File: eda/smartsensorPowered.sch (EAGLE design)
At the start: 36 parts, among them Q1 IRFML8244, Q2 IRFML8244, Q3 IRFML8244, Q4 IRFML8244, U1 ISL83491SOIC, U2 ATTINY1634

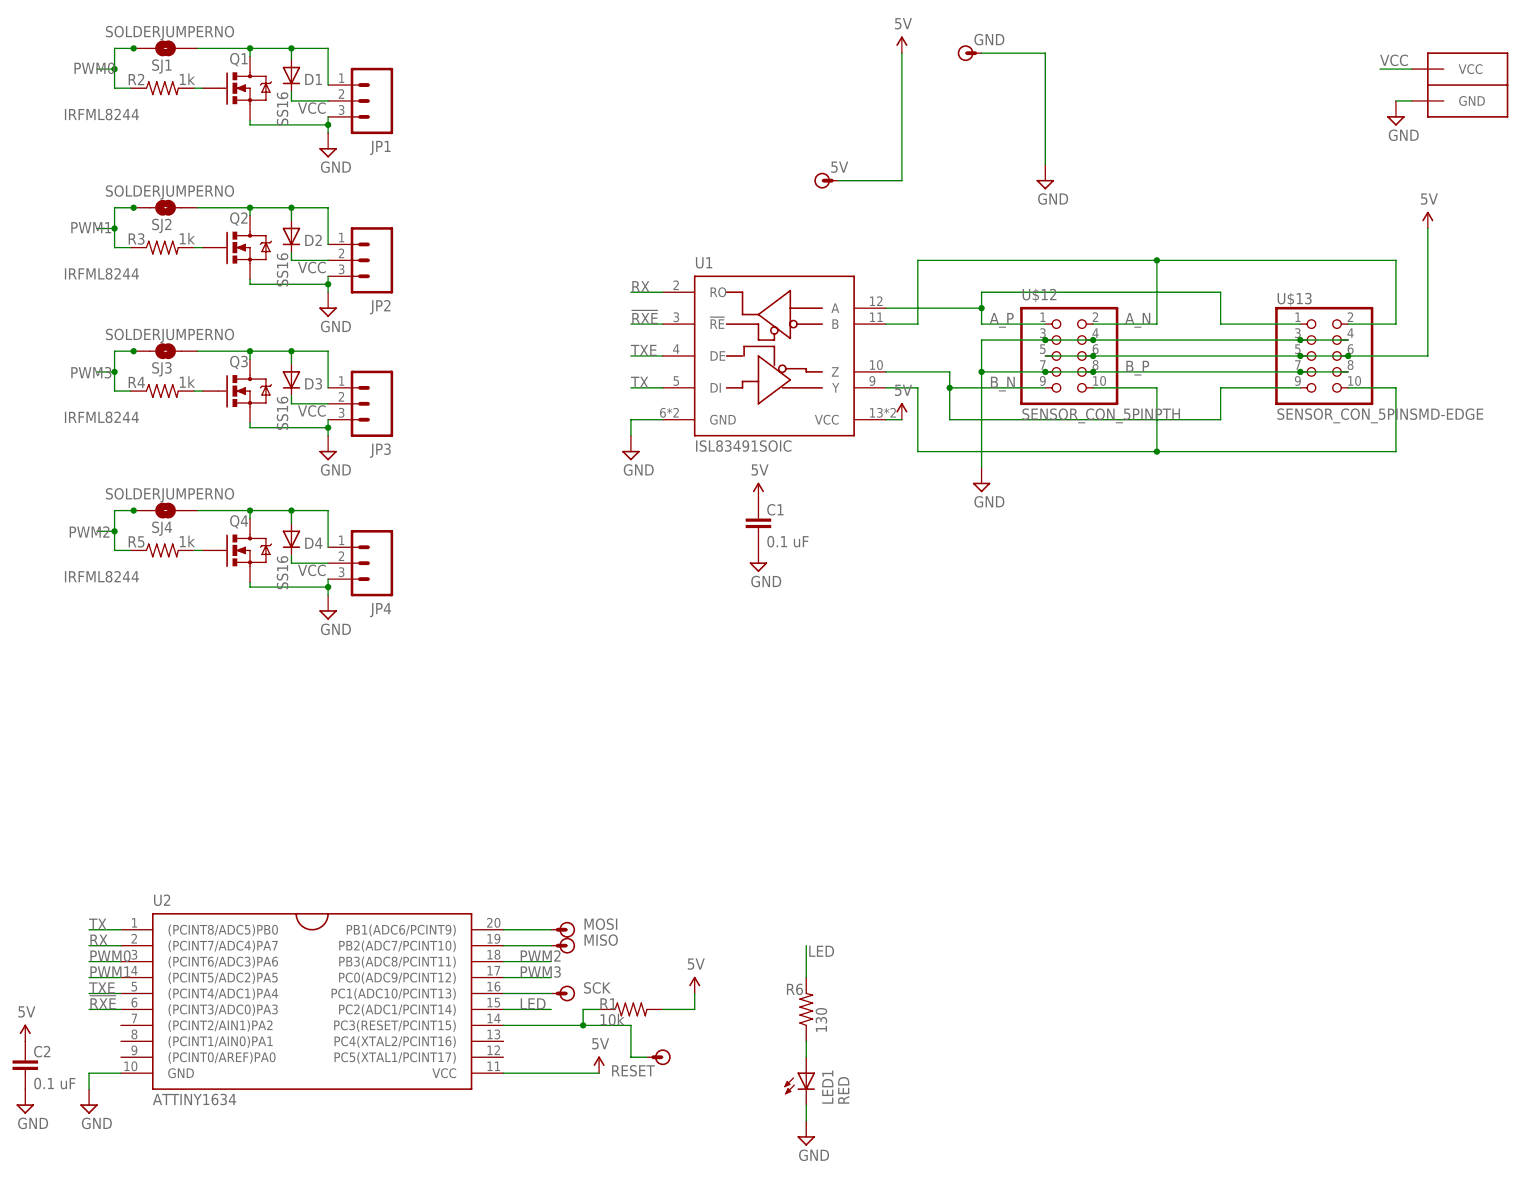
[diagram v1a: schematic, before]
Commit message: Add koala buck regulator to powered smart device and update everything for version 4
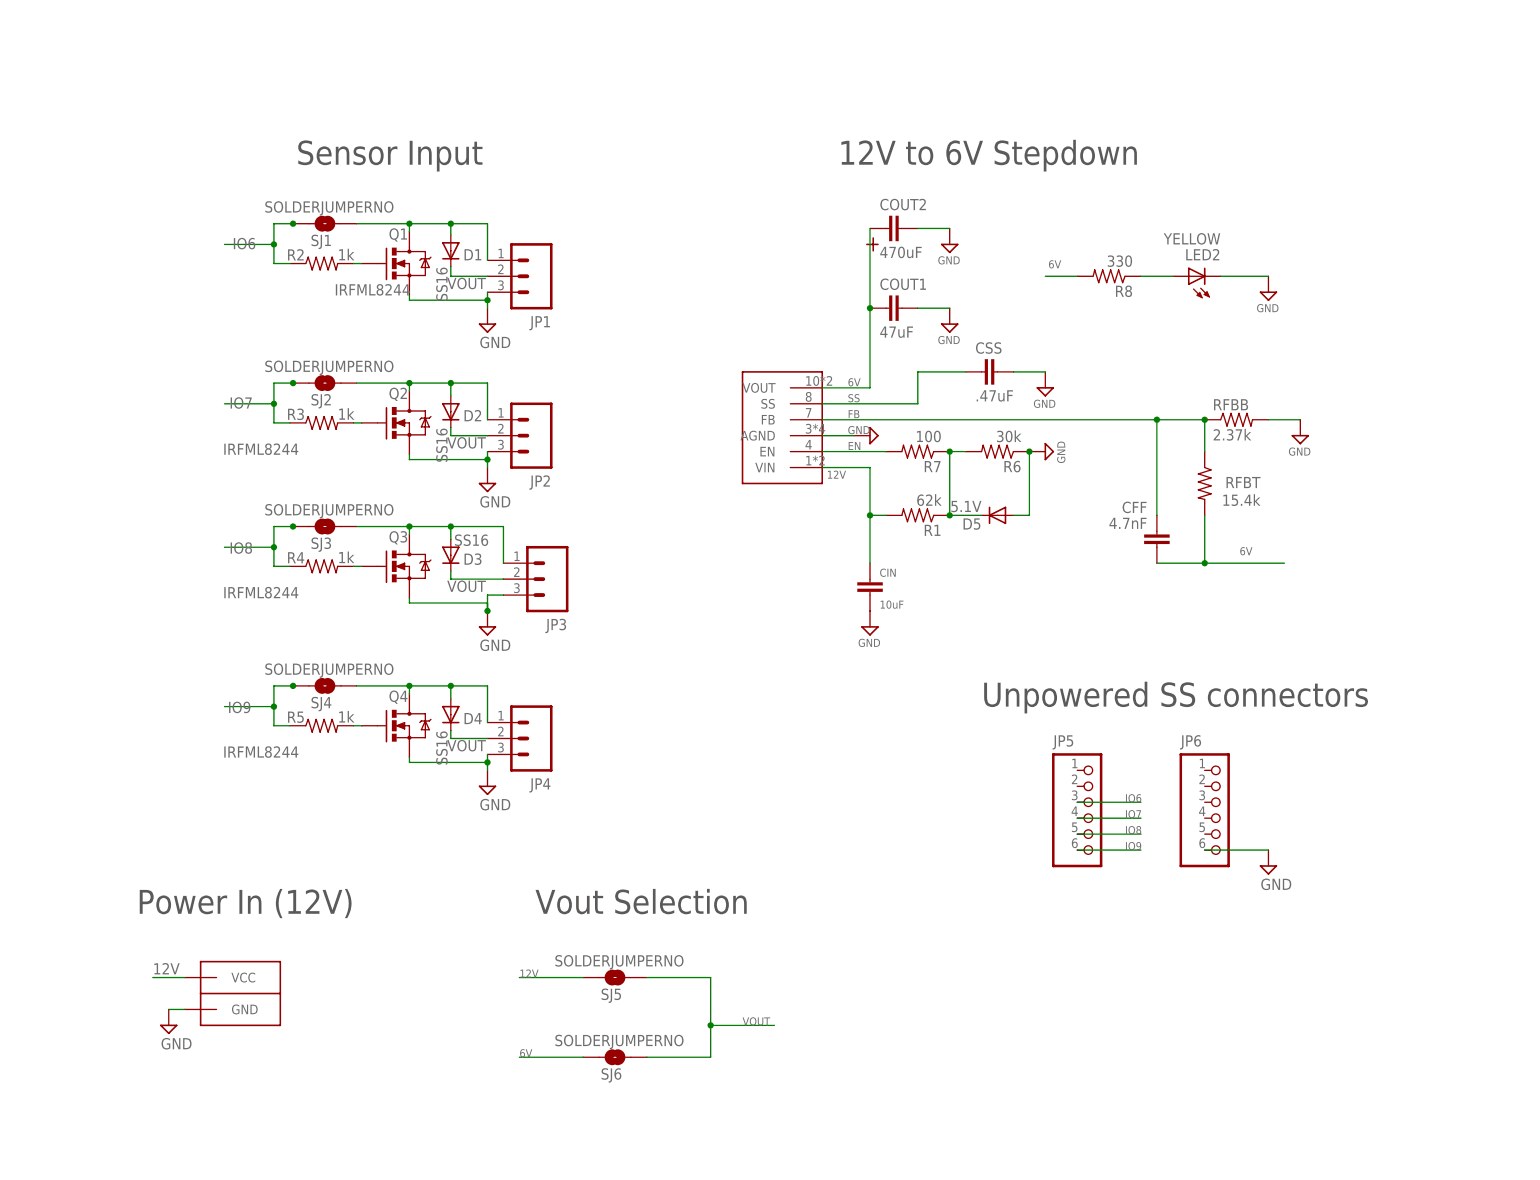
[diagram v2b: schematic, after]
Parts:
- removed 5V, GND, MISO, MOSI, RESET, SCK: (no value), pie:POGO_PIN
- removed C1, C2: 0.1 uF, pie:CAP0603-CAP
- removed LED1: RED, pie:LED0805
- removed U$12: SENSOR_CON_5PINPTH, pie:SENSOR_CON_5PINPTH-SHROUDED
- removed U$13: SENSOR_CON_5PINSMD-EDGE, pie:SENSOR_CON_5PINSMD-EDGE
- removed U1: ISL83491SOIC, pie:ISL83491SOIC
- removed U2: ATTINY1634, pie:ATTINY1634
- added CFF: 4.7nF, pie:CAP0603-CAP
- added CIN: 10uF, pie:CAP1206
- added COUT1: 47uF, pie:CAP1206
- added COUT2: 470uF, pie:TANT_CASE_E
- added CSS: .47uF, pie:CAP0603-CAP
- added D5: 5.1V, pie:DIODESOD-323
- added JP5, JP6: (no value), pie:PINHD-1X6
- added LED2: YELLOW, pie:LED0805
- added R7: 100, pie:R-US_R0603
- added R8: 330, pie:R-US_R0603
- added RFBB: 2.37k, pie:R-US_R0603
- added RFBT: 15.4k, pie:R-US_R0603
- added SJ5, SJ6: SOLDERJUMPERNO, pie:SOLDERJUMPERNO
- added U$3: LMZ12010, pie:LMZ12010
- R1: value 10k -> 62k
- R6: value 130 -> 30k
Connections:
- removed net !RXE: U1.!RE, U2.(PCINT3/ADC0)PA3
- removed net 5V: 5V.P$1, C1.1, C2.1, R1.2, U$12.5, U$12.6, U$13.5, U$13.6, U1.VCC, U2.VCC
- removed net A_N: U$12.2, U$13.2, U1.B
- removed net A_P: U$12.1, U$13.1, U1.A
- removed net B_N: U$12.9, U$13.9, U1.Z
- removed net B_P: U$12.10, U$13.10, U1.Y
- removed net LED: R6.2, U2.PC2(ADC1/PCINT14)
- removed net N$12: SCK.P$1, U2.PC1(ADC10/PCINT13)
- removed net N$6: MOSI.P$1, U2.PB1(ADC6/PCINT9)
- removed net N$9: MISO.P$1, U2.PB2(ADC7/PCINT10)
- removed net PWM0: R2.1, SJ1.1, U2.(PCINT6/ADC3)PA6
- removed net PWM1: R3.1, SJ2.1, U2.(PCINT5/ADC2)PA5
- removed net PWM2: R5.1, SJ4.1, U2.PB3(ADC8/PCINT11)
- removed net PWM3: R4.1, SJ3.1, U2.PC0(ADC9/PCINT12)
- removed net RESET: R1.1, RESET.P$1, U2.PC3(RESET/PCINT15)
- removed net RX: U1.RO, U2.(PCINT7/ADC4)PA7
- removed net TX: U1.DI, U2.(PCINT8/ADC5)PB0
- removed net TXE: U1.DE, U2.(PCINT4/ADC1)PA4
- removed net VCC: CONN1.VCC, D1.C, D2.C, D3.C, D4.C, JP1.2, JP2.2, JP3.2, JP4.2
- new net 12V: CIN.1, CONN1.VCC, R1.2, SJ5.1, U$3.VIN
- new net 6V: CFF.1, COUT1.1, COUT2.POS, R8.2, RFBT.2, SJ6.1, U$3.VOUT
- new net DIODE: D5.C, R1.1, R6.2, R7.1
- new net EN: R7.2, U$3.EN
- new net FB: CFF.2, RFBB.1, RFBT.1, U$3.FB
- new net IO6: JP5.3, R2.1, SJ1.1
- new net IO7: JP5.4, R3.1, SJ2.1
- new net IO8: JP5.5, R4.1, SJ3.1
- new net IO9: JP5.6, R5.1, SJ4.1
- new net SS: CSS.1, U$3.SS
- new net VOUT: D1.C, D2.C, D3.C, D4.C, JP1.2, JP2.2, JP3.2, JP4.2, SJ5.2, SJ6.2
- net GND: now also CIN.2, COUT1.2, COUT2.NEG, CSS.2, D5.A, JP6.6, LED2.C, R6.1, RFBB.2, U$3.AGND; no longer C1.2, C2.2, GND.P$1, LED1.C, U$12.3, U$12.4, U$12.7, U$12.8, U$13.3, U$13.4, U$13.7, U$13.8, U1.GND, U2.GND
- net N$3: now also LED2.A, R8.1; no longer LED1.A, R6.1
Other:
- note added: "12V to 6V Stepdown"
- note added: "Power In (12V)"
- note added: "Sensor Input"
- note added: "Unpowered SS connectors"
- note added: "Vout Selection"
- moved on the sheet: D1, D2, D3, D4, JP1, JP2, JP3, JP4, Q1, Q2, Q3, Q4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

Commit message: Fix smartsensorPowered brd and sch #2 - renamed N$1 N$2 N$3 N$4 wires with 6V_IF_SERVO1 6V_If_SERVO2 and so on - ripped up the trace from cout1 to GND -
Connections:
- net N$1 renamed 6V_IF_SERVO1
- net N$10 renamed 6V_IF_SERVO4
- net N$4 renamed 6V_IF_SERVO2
- net N$7 renamed 6V_IF_SERVO3
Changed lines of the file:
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@@
 </segment>
 </net>
-<net name="N$1" class="0">
+<net name="6V_IF_SERVO1" class="0">
 <segment>
 <pinref part="JP1" gate="G$1" pin="1"/>
@@
 </segment>
 </net>
-<net name="N$4" class="0">
+<net name="6V_IF_SERVO2" class="0">
 <segment>
 <pinref part="JP2" gate="G$1" pin="1"/>
@@
 </segment>
 </net>
-<net name="N$7" class="0">
+<net name="6V_IF_SERVO3" class="0">
 <segment>
 <pinref part="JP3" gate="G$1" pin="1"/>
@@
 </segment>
 </net>
-<net name="N$10" class="0">
+<net name="6V_IF_SERVO4" class="0">
 <segment>
 <pinref part="JP4" gate="G$1" pin="1"/>

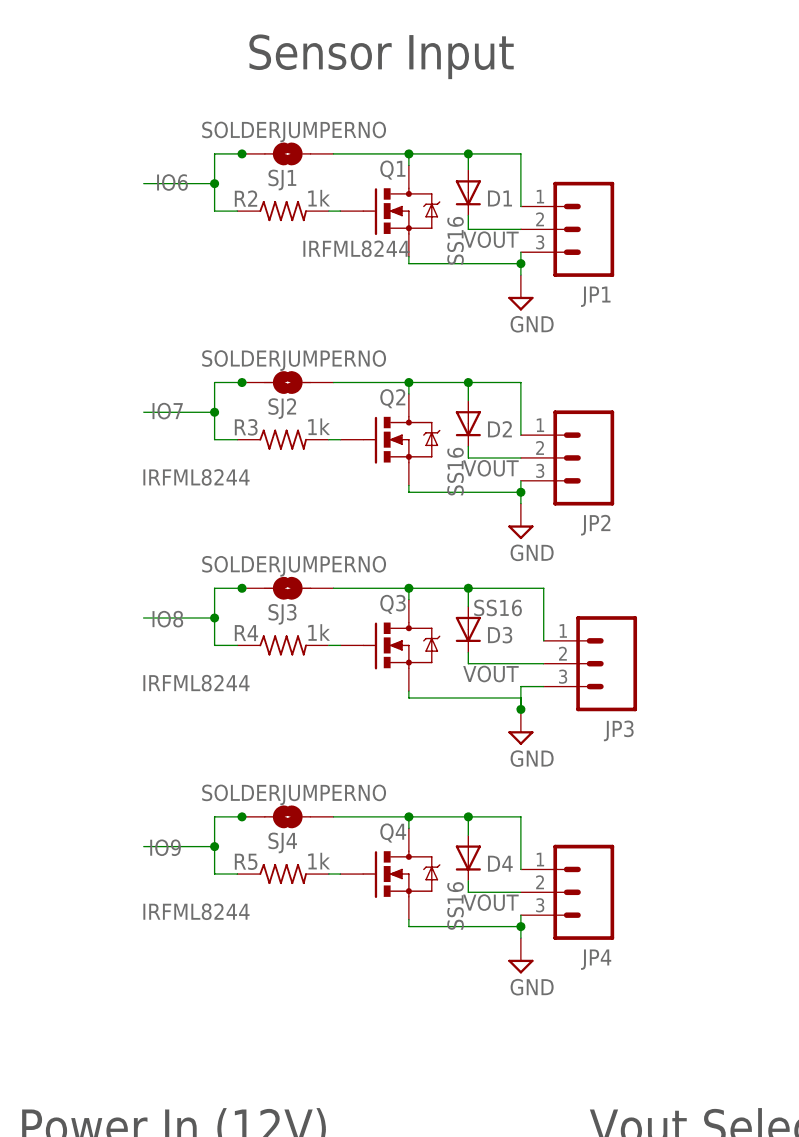
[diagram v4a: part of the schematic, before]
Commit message: Fix for smartsensorPowered .brd .sch #2 - Changed the name of N$1 N$2 N$S N$4 to 6V_IF_SERVO1/2/3/4 - Ripped up redundant wire from cout1 - Casey explained that Vout connected by a polygon to a bottom layer is   appropriate - cleaned up the schematic so the parts do not overlap
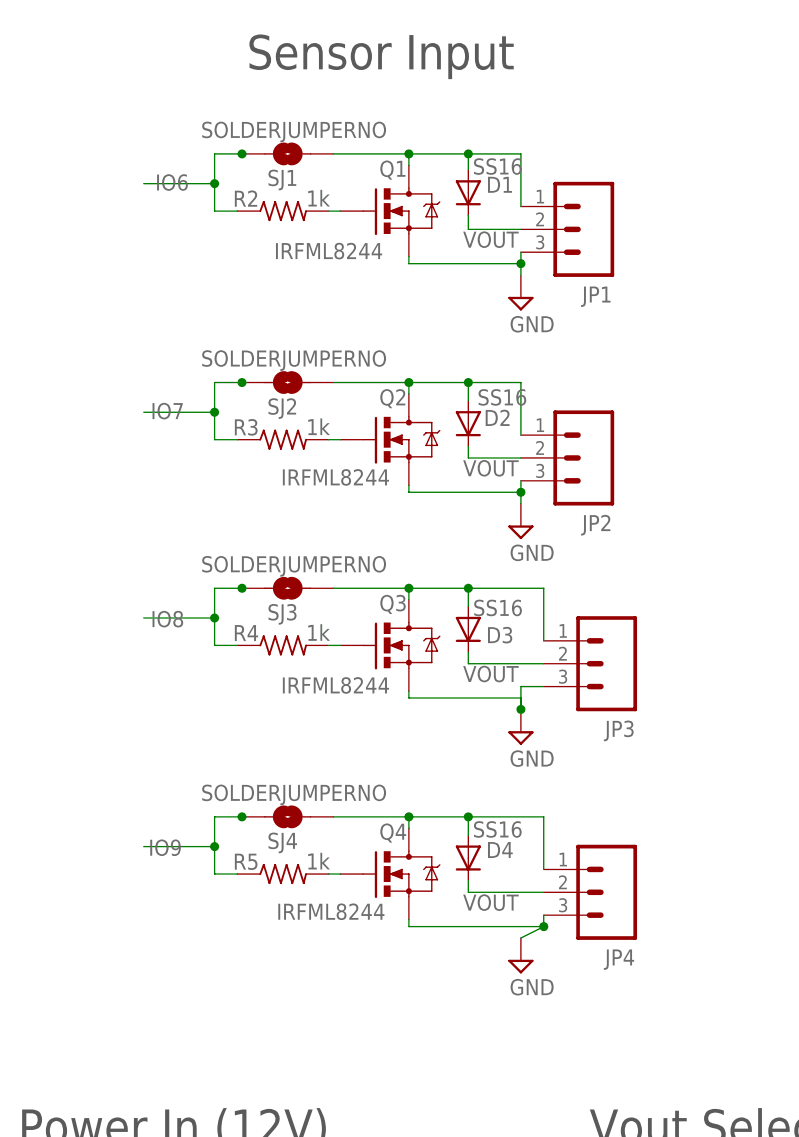
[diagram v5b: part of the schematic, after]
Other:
- moved on the sheet: JP4
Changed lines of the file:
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@@
 <part name="FRAME1" library="pie" deviceset="FRAME-LETTER" device="">
 <attribute name="AUTHOR" value="Vincent D, Devin H, Kate R, Andrew H, Sumita G, Tobin H, Casey D."/>
-<attribute name="REVISION" value="4B"/>
+<attribute name="REVISION" value="4C"/>
 </part>
 <part name="SUPPLY10" library="pie" deviceset="GND" device=""/>
@@
 <instance part="Q1" gate="G$1" x="66.294" y="144.272" smashed="yes">
 <attribute name="NAME" x="62.992" y="148.082" size="1.778" layer="95" font="vector"/>
-<attribute name="VALUE" x="54.356" y="139.192" size="1.778" layer="96" font="vector"/>
+<attribute name="VALUE" x="51.308" y="138.938" size="1.778" layer="96" font="vector"/>
 </instance>
 <instance part="D4" gate="G$1" x="72.898" y="72.39" smashed="yes" rot="R270">
-<attribute name="NAME" x="77.9526" y="72.644" size="1.778" layer="95" font="vector" rot="R180"/>
-<attribute name="VALUE" x="70.5866" y="69.85" size="1.778" layer="96" font="vector" rot="R270"/>
+<attribute name="NAME" x="77.9526" y="74.168" size="1.778" layer="95" font="vector" rot="R180"/>
+<attribute name="VALUE" x="73.3806" y="74.676" size="1.778" layer="96" font="vector"/>
 </instance>
 <instance part="JP1" gate="G$1" x="86.36" y="142.24" rot="R180"/>
@@
 <instance part="Q2" gate="G$1" x="66.294" y="118.872" smashed="yes">
 <attribute name="NAME" x="62.992" y="122.682" size="1.778" layer="95" font="vector"/>
-<attribute name="VALUE" x="36.576" y="113.792" size="1.778" layer="96" font="vector"/>
+<attribute name="VALUE" x="52.07" y="113.792" size="1.778" layer="96" font="vector"/>
 </instance>
 <instance part="D1" gate="G$1" x="72.898" y="146.304" smashed="yes" rot="R270">
-<attribute name="NAME" x="77.9526" y="146.558" size="1.778" layer="95" font="vector" rot="R180"/>
-<attribute name="VALUE" x="70.5866" y="143.764" size="1.778" layer="96" font="vector" rot="R270"/>
+<attribute name="NAME" x="77.9526" y="148.082" size="1.778" layer="95" font="vector" rot="R180"/>
+<attribute name="VALUE" x="73.3806" y="148.336" size="1.778" layer="96" font="vector"/>
 </instance>
 <instance part="JP2" gate="G$1" x="86.36" y="116.84" rot="R180"/>
@@
 <instance part="Q3" gate="G$1" x="66.294" y="96.012" smashed="yes">
 <attribute name="NAME" x="62.992" y="99.822" size="1.778" layer="95" font="vector"/>
-<attribute name="VALUE" x="36.576" y="90.932" size="1.778" layer="96" font="vector"/>
+<attribute name="VALUE" x="52.07" y="90.678" size="1.778" layer="96" font="vector"/>
 </instance>
 <instance part="D2" gate="G$1" x="72.898" y="120.65" smashed="yes" rot="R270">
-<attribute name="NAME" x="77.9526" y="120.904" size="1.778" layer="95" font="vector" rot="R180"/>
-<attribute name="VALUE" x="70.5866" y="118.11" size="1.778" layer="96" font="vector" rot="R270"/>
+<attribute name="NAME" x="77.6986" y="122.174" size="1.778" layer="95" font="vector" rot="R180"/>
+<attribute name="VALUE" x="73.8886" y="122.682" size="1.778" layer="96" font="vector"/>
 </instance>
 <instance part="JP3" gate="G$1" x="88.9" y="93.98" rot="R180"/>
@@
 <instance part="Q4" gate="G$1" x="66.294" y="70.612" smashed="yes">
 <attribute name="NAME" x="62.992" y="74.422" size="1.778" layer="95" font="vector"/>
-<attribute name="VALUE" x="36.576" y="65.532" size="1.778" layer="96" font="vector"/>
+<attribute name="VALUE" x="51.562" y="65.532" size="1.778" layer="96" font="vector"/>
 </instance>
 <instance part="D3" gate="G$1" x="72.898" y="97.79" smashed="yes" rot="R270">
@@
 <attribute name="VALUE" x="73.406" y="99.2886" size="1.778" layer="96" font="vector"/>
 </instance>
-<instance part="JP4" gate="G$1" x="86.36" y="68.58" rot="R180"/>
+<instance part="JP4" gate="G$1" x="88.9" y="68.58" rot="R180"/>
 <instance part="SJ4" gate="1" x="52.832" y="76.962" smashed="yes">
 <attribute name="NAME" x="50.546" y="73.406" size="1.778" layer="95" font="vector"/>
@@
 <pinref part="JP4" gate="G$1" pin="3"/>
 <pinref part="SUPPLY9" gate="GND" pin="GND"/>
-<wire x1="78.74" y1="66.04" x2="78.74" y2="64.77" width="0.1524" layer="91"/>
+<wire x1="81.28" y1="66.04" x2="81.28" y2="64.77" width="0.1524" layer="91"/>
 <pinref part="Q4" gate="G$1" pin="S"/>
-<wire x1="78.74" y1="64.77" x2="78.74" y2="63.5" width="0.1524" layer="91"/>
+<wire x1="81.28" y1="64.77" x2="78.74" y2="63.5" width="0.1524" layer="91"/>
 <wire x1="66.294" y1="65.532" x2="66.294" y2="64.77" width="0.1524" layer="91"/>
-<wire x1="66.294" y1="64.77" x2="78.74" y2="64.77" width="0.1524" layer="91"/>
-<junction x="78.74" y="64.77"/>
+<wire x1="66.294" y1="64.77" x2="81.28" y2="64.77" width="0.1524" layer="91"/>
+<junction x="81.28" y="64.77"/>
 </segment>
 <segment>
@@
 <segment>
 <pinref part="JP4" gate="G$1" pin="1"/>
-<wire x1="78.74" y1="71.12" x2="78.74" y2="76.962" width="0.1524" layer="91"/>
+<wire x1="81.28" y1="71.12" x2="81.28" y2="76.962" width="0.1524" layer="91"/>
 <pinref part="Q4" gate="G$1" pin="D"/>
 <wire x1="66.294" y1="75.692" x2="66.294" y2="76.962" width="0.1524" layer="91"/>
 <wire x1="66.294" y1="76.962" x2="72.898" y2="76.962" width="0.1524" layer="91"/>
 <pinref part="SJ4" gate="1" pin="2"/>
-<wire x1="72.898" y1="76.962" x2="78.74" y2="76.962" width="0.1524" layer="91"/>
+<wire x1="72.898" y1="76.962" x2="81.28" y2="76.962" width="0.1524" layer="91"/>
 <wire x1="57.912" y1="76.962" x2="66.294" y2="76.962" width="0.1524" layer="91"/>
 <junction x="66.294" y="76.962"/>
@@
 <pinref part="JP4" gate="G$1" pin="2"/>
 <label x="78.486" y="68.326" size="1.778" layer="95" font="vector" rot="R180"/>
-<wire x1="78.74" y1="68.58" x2="72.898" y2="68.58" width="0.1524" layer="91"/>
+<wire x1="81.28" y1="68.58" x2="72.898" y2="68.58" width="0.1524" layer="91"/>
 <pinref part="D4" gate="G$1" pin="C"/>
 <wire x1="72.898" y1="69.85" x2="72.898" y2="68.58" width="0.1524" layer="91"/>
